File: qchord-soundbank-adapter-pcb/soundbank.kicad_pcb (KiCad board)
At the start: 2 copper layers, 32 x 47.5 mm, 2 parts, among them U1 8MB ROM, U2 8MB Flash

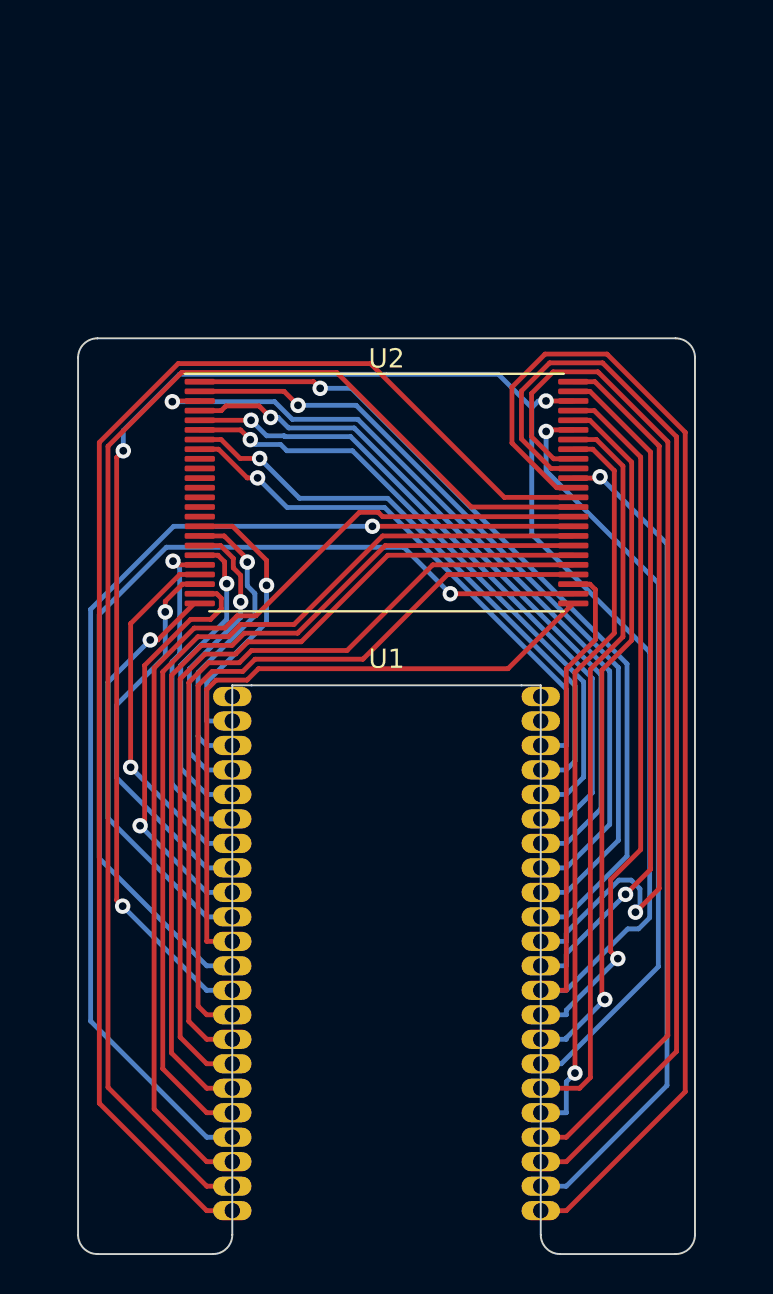
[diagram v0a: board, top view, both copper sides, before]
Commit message: Flip outtie to innie
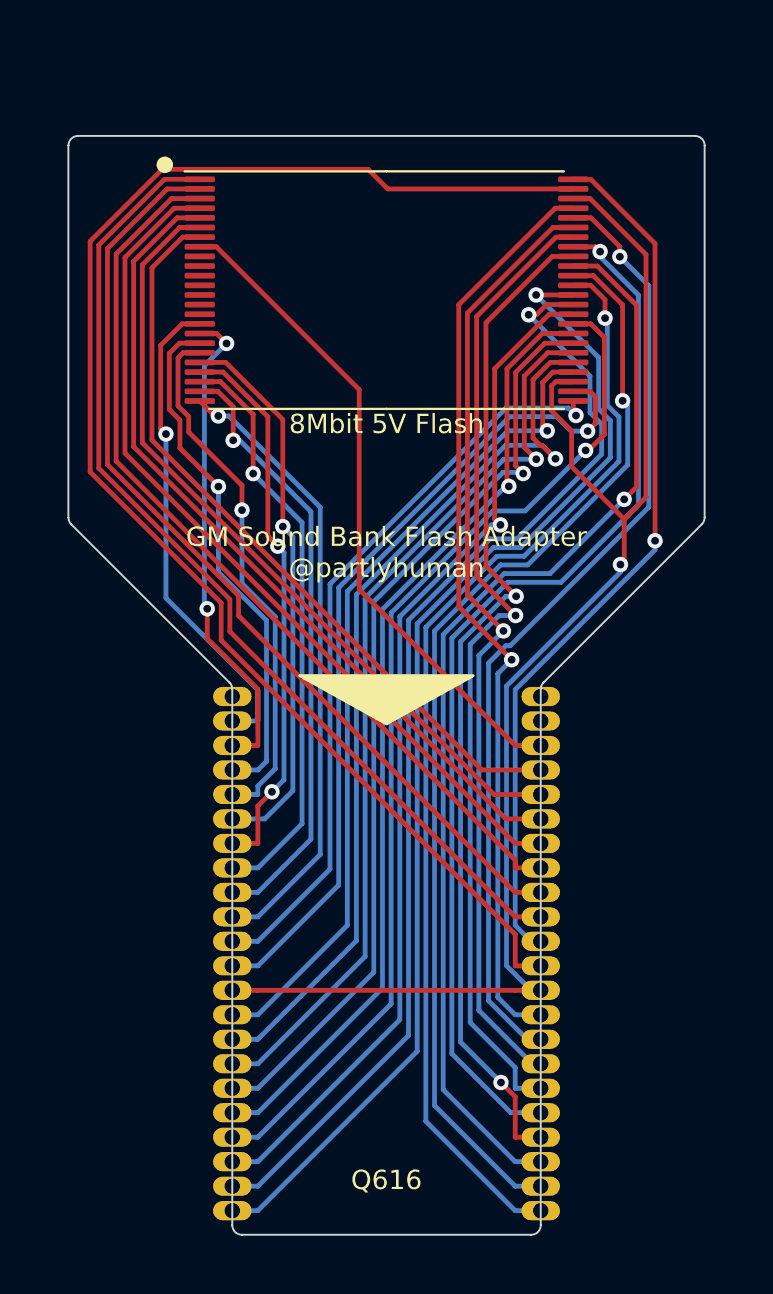
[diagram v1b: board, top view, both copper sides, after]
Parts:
- U2: value 8MB Flash -> 8Mbit 5V Flash
- moved U2 10.5 mm to (94.5, 43.0)
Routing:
- net /GND: track 118.1 -> 72.9 mm, vias 3 -> 1
- net /BYTE: track 35.1 -> 75.1 mm, vias 1 -> 0
- net /Q13: track 38.3 -> 55.4 mm
- net /Q4: track 43.1 -> 57.0 mm
- net /Q7: track 36.7 -> 49.9 mm
- net /Q6: track 38.4 -> 51.4 mm, vias 0 -> 1
- net /Q11: track 72.6 -> 60.7 mm, vias 0 -> 1
- net /Q3: track 70.4 -> 58.8 mm, vias 0 -> 1
- net /A5: track 17.2 -> 28.8 mm
- net /Q15: track 36.7 -> 48.0 mm
- net /A6: track 16.4 -> 27.7 mm
- net /A7: track 16.0 -> 27.0 mm
- net /A1: track 22.1 -> 32.4 mm
- net /A18: track 15.1 -> 25.4 mm
- net /A3: track 20.3 -> 30.3 mm
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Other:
- board size 32 x 47.5 mm -> 33 x 57 mm
- board text added: "GM Sound Bank Flash Adapter @partlyhuman"
- board text added: "Q616"

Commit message: Makes room for neighboring IC
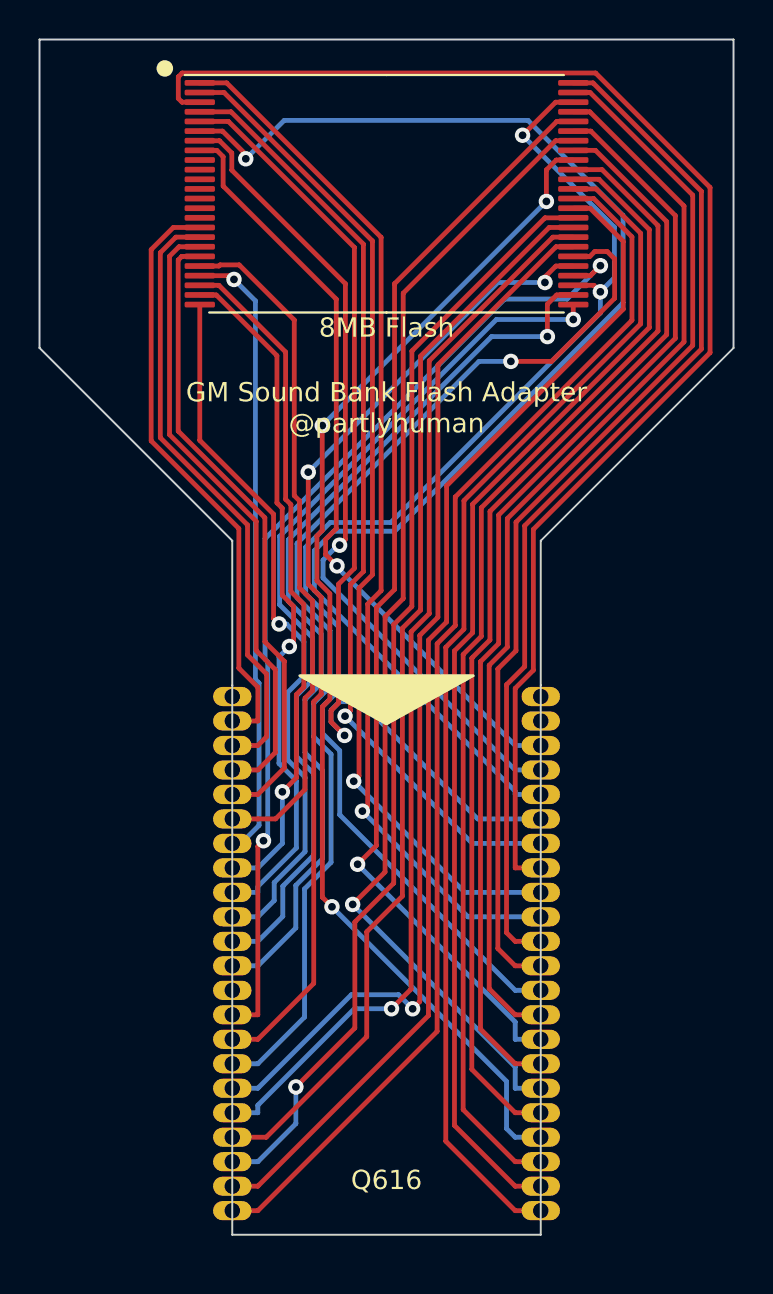
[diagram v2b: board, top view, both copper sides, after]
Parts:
- U2: value 8Mbit 5V Flash -> 8MB Flash
- moved U2 5.00 mm to (94.5, 38.0)
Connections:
- U1 pad 13: /GND -> unconnected-(U1-GND-Pad13)
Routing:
- net /A10: track 41.2 -> 69.7 mm, vias 0 -> 1
- net /A13: track 47.3 -> 73.2 mm
- net /BYTE: track 75.1 -> 54.3 mm
- net /Q8: track 47.3 -> 57.5 mm
- net /Q5: track 52.9 -> 62.6 mm, vias 2 -> 3
- net /A11: track 43.1 -> 52.0 mm, vias 0 -> 1
- net /Q14: track 49.2 -> 57.4 mm, vias 1 -> 0
- net /A16: track 45.7 -> 53.6 mm, vias 1 -> 0
- net /Q6: track 51.4 -> 59.2 mm
- net /Q15: track 48.0 -> 55.8 mm, vias 1 -> 0
- net /OE: track 43.4 -> 51.2 mm, vias 1 -> 2
- net /Q7: track 49.9 -> 57.5 mm
- net /A0: track 38.9 -> 45.6 mm
- net /A5: track 28.8 -> 35.4 mm, vias 1 -> 0
- net /GND: track 72.9 -> 66.2 mm, vias 1 -> 2
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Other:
- board size 33 x 57 mm -> 36 x 62 mm

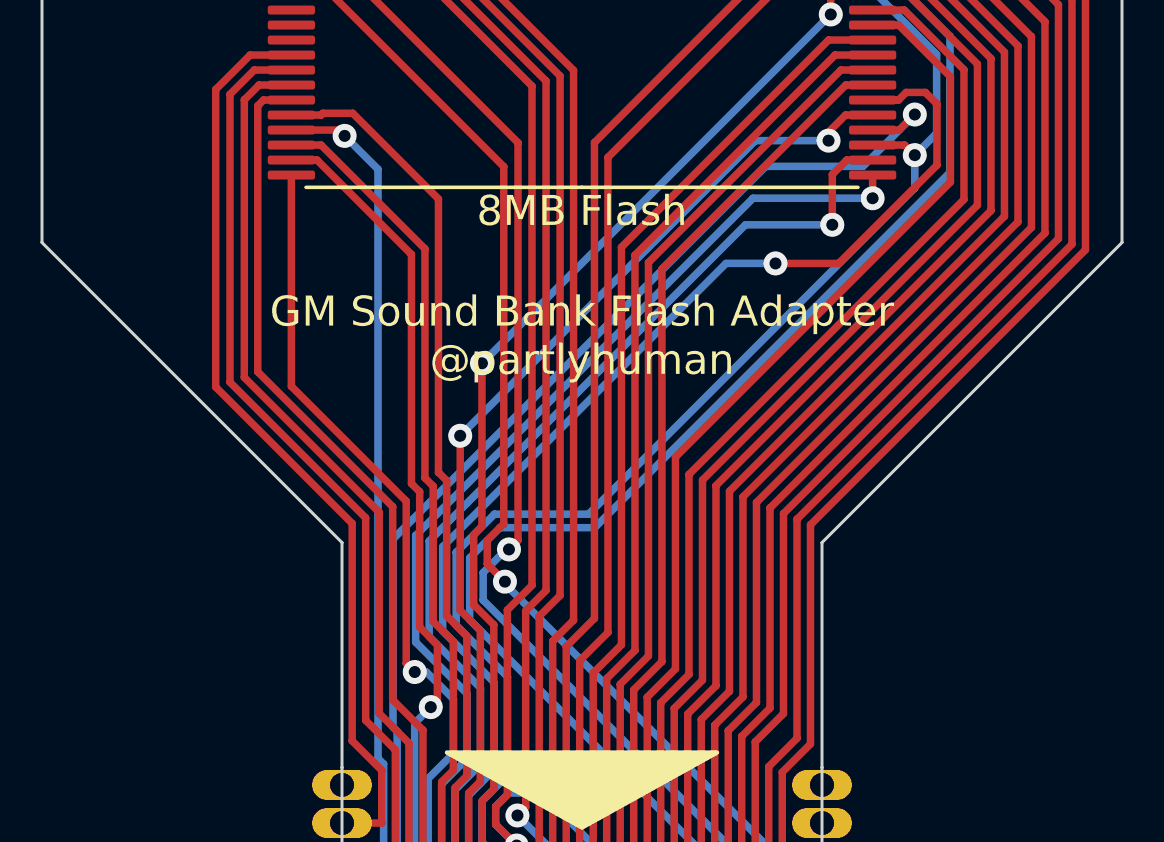
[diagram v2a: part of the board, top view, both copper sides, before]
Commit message: Comic sans to match mainboard
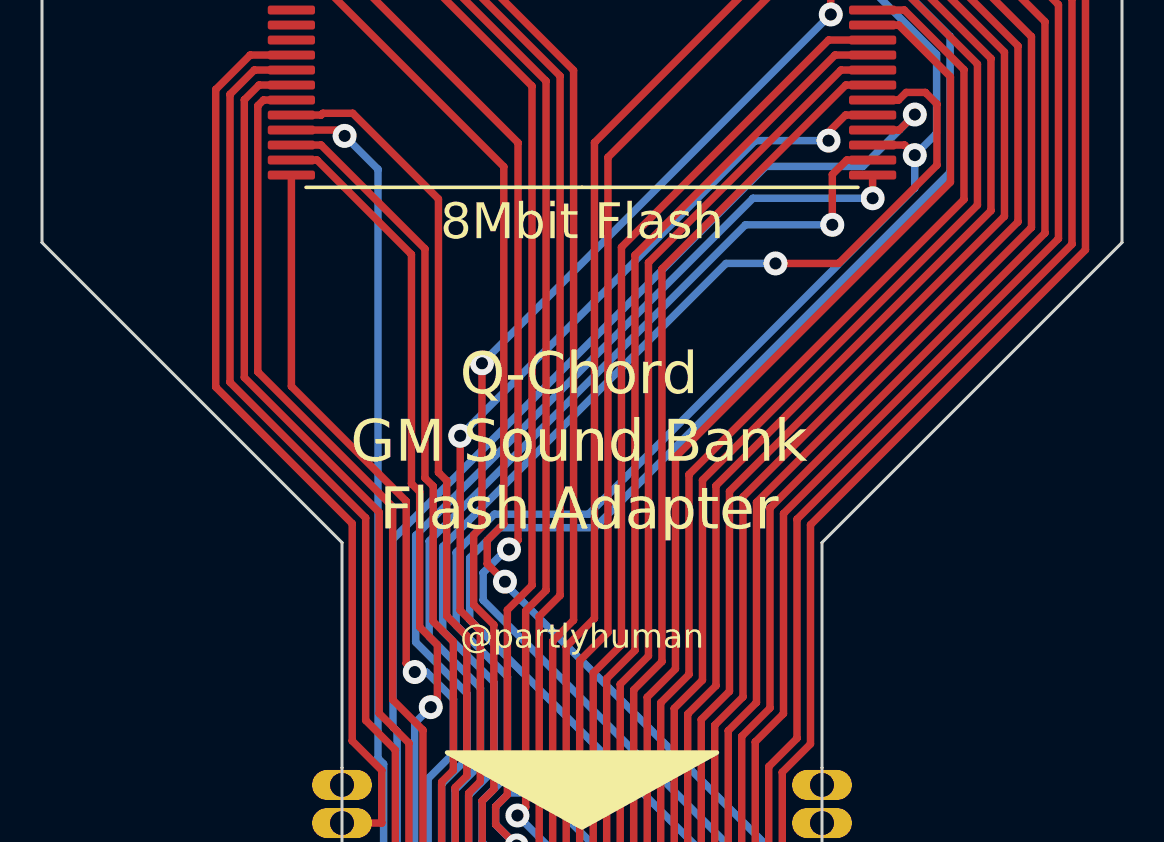
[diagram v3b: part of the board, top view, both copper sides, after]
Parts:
- U2: value 8MB Flash -> 8Mbit Flash
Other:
- board text added: "@partlyhuman"
- board text added: "Q-Chord GM Sound Bank Flash Adapter"
- board text removed: "GM Sound Bank Flash Adapter @partlyhuman"

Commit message: Redesign in-place
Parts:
- moved U2 39.4 mm to (94.5, 77.4), turned to -90 degrees
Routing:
- net /A13: track 73.2 -> 7.75 mm, vias 0 -> 1
- net /A10: track 69.7 -> 6.61 mm
- net /Q5: track 62.6 -> 8.09 mm, vias 3 -> 1
- net /Q11: track 63.7 -> 10.1 mm
- net /Q3: track 61.5 -> 8.95 mm
- net /Q4: track 61.5 -> 9.28 mm
- net /VCC: track 62.2 -> 10.1 mm
- net /Q12: track 60.8 -> 8.85 mm
- net /Q6: track 59.2 -> 7.60 mm
- net /Q13: track 59.0 -> 7.48 mm, vias 0 -> 1
- net /Q10: track 57.9 -> 8.22 mm, vias 1 -> 0
- net /Q7: track 57.5 -> 8.38 mm
- net /Q8: track 57.5 -> 8.63 mm
- net /Q2: track 56.3 -> 8.10 mm
- net /Q1: track 55.2 -> 7.63 mm
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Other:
- board size 36 x 62 mm -> 16 x 29.7 mm

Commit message: Don't leave stuff floating
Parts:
- U1: value 8MB ROM -> 8Mbit ROM
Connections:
- U2 pad 11: unconnected-(U2-~{WE}-Pad11) -> /BYTE
- U2 pad 12: unconnected-(U2-~{RESET}-Pad12) -> /BYTE
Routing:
- net /BYTE: track 11.0 -> 24.2 mm, vias 1 -> 0
- net /A2: track 8.54 -> 14.6 mm, vias 0 -> 1
- net /Q13: track 7.48 -> 13.4 mm
- net /Q5: track 8.09 -> 12.6 mm
- net /Q2: track 8.10 -> 12.2 mm, vias 0 -> 1
- net /Q15: track 9.11 -> 12.0 mm, vias 1 -> 0
- net /A6: track 6.21 -> 9.08 mm, vias 1 -> 0
- net /Q14: track 10.4 -> 7.56 mm, vias 0 -> 1
- net /OE: track 9.27 -> 12.0 mm, vias 1 -> 0
- net /A13: track 7.75 -> 10.2 mm, vias 1 -> 0
- net /GND: track 24.3 -> 22.3 mm
- net /A5: track 8.68 -> 6.93 mm, vias 0 -> 1
- net /Q9: track 8.90 -> 8.03 mm
- net /Q6: track 7.60 -> 8.45 mm
- net /A8: track 7.20 -> 7.96 mm
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
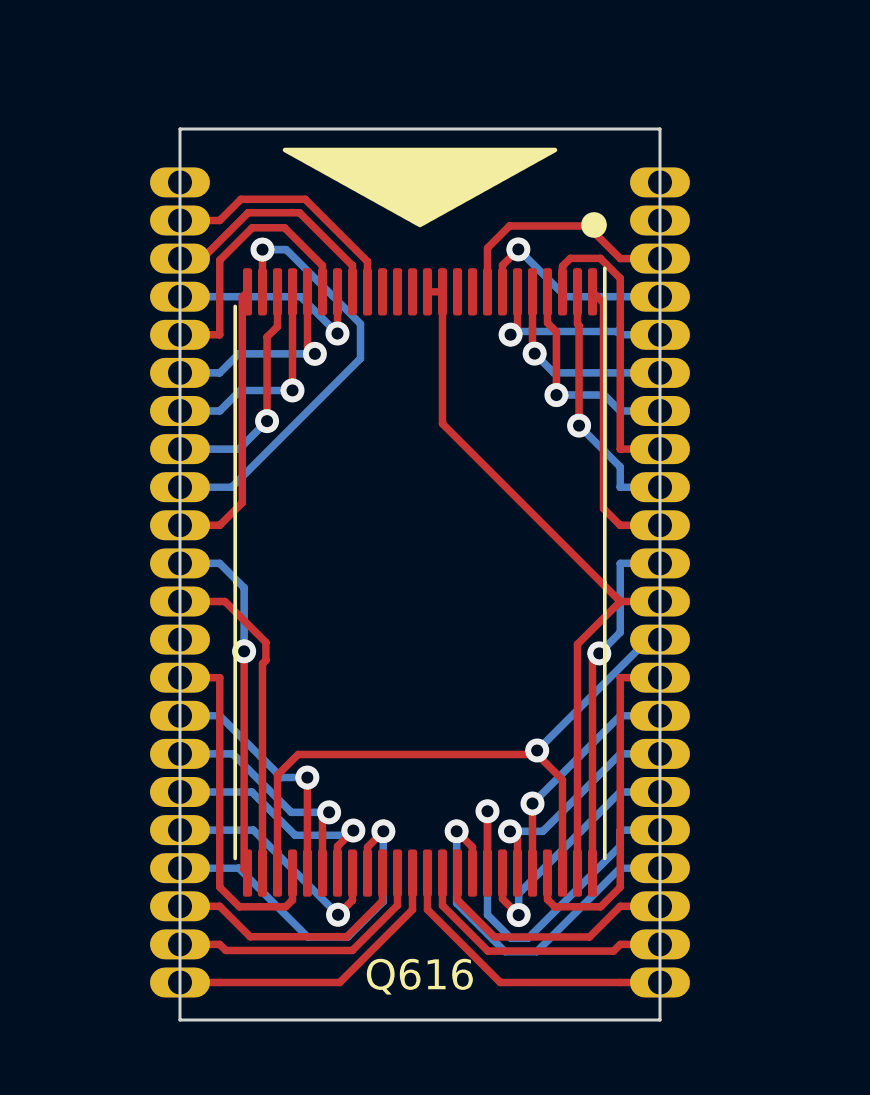
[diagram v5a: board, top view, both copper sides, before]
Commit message: add extra GND
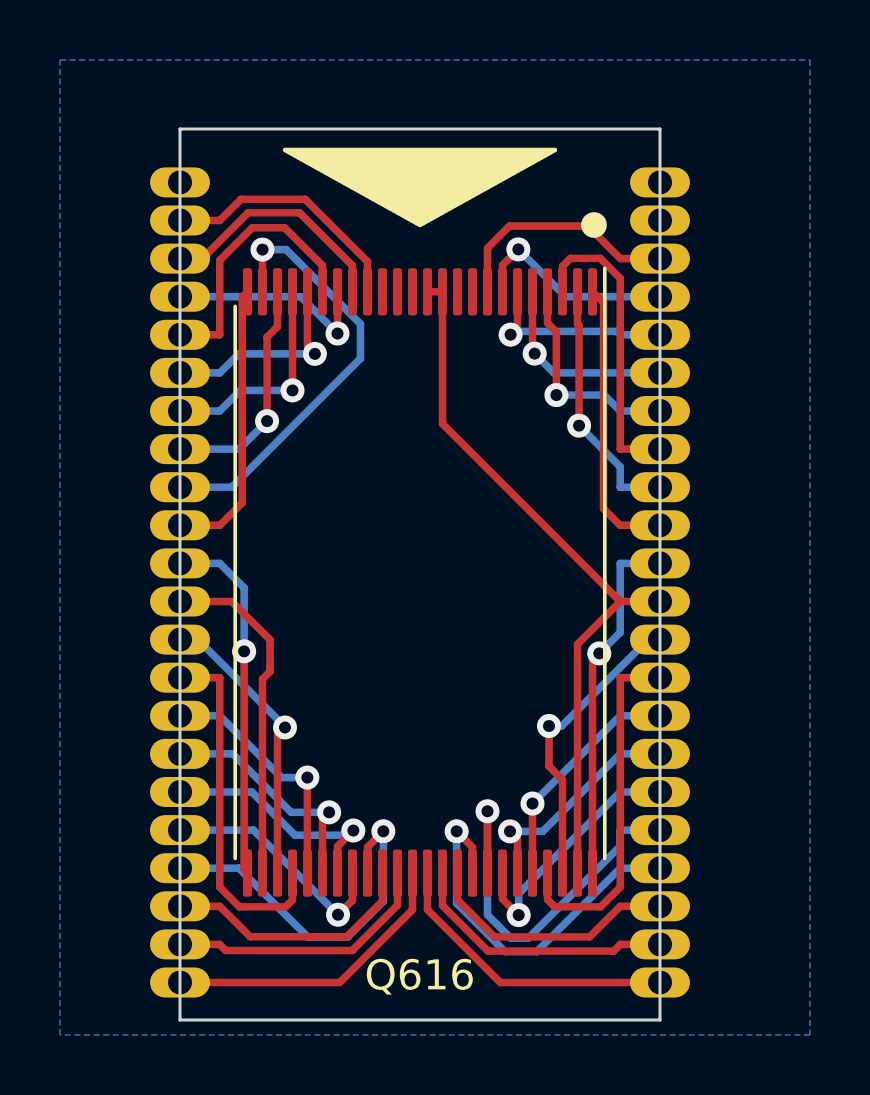
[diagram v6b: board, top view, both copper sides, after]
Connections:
- U1 pad 13: unconnected-(U1-GND-Pad13) -> /GND
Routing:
- net /GND: track 22.3 -> 19.7 mm, vias 1 -> 2
- added copper zone on B.Cu, net /GND
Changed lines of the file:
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@@
   (net 47 "unconnected-(U2-Pad14)")
   (net 48 "unconnected-(U2-~{RY{slash}BY}-Pad15)")
-  (net 49 "unconnected-(U1-GND-Pad13)")
   (footprint "Package_SO:TSOP-I-48_18.4x12mm_P0.5mm" (layer "F.Cu")
     (at 94.5 77.415 -90)
@@
       (net 12 "/CE") (pinfunction "~{CE}") (pintype "input"))
     (pad "13" thru_hole oval (at -8 1.905) (size 2 1) (drill 0.8) (property pad_prop_castellated) (layers "*.Cu" "*.Mask")
-      (net 49 "unconnected-(U1-GND-Pad13)") (pinfunction "GND") (pintype "input+no_connect"))
+      (net 13 "/GND") (pinfunction "GND") (pintype "input"))
     (pad "14" thru_hole oval (at -8 3.175) (size 2 1) (drill 0.8) (property pad_prop_castellated) (layers "*.Cu" "*.Mask")
       (net 14 "/OE") (pinfunction "~{OE}") (pintype "input"))
@@
   (segment (start 86.5 76.78) (end 87.8251 76.78) (width 0.25) (layer "B.Cu") (net 11))
   (segment (start 88.6378 79.712) (end 88.6378 77.5927) (width 0.25) (layer "B.Cu") (net 11))
-  (segment (start 86.5 78.05) (end 87.8251 78.05) (width 0.25) (layer "F.Cu") (net 12))
-  (segment (start 89.25 80.1253) (end 89.3629 80.0124) (width 0.25) (layer "F.Cu") (net 12))
-  (segment (start 89.3629 80.0124) (end 89.3629 79.4116) (width 0.25) (layer "F.Cu") (net 12))
-  (segment (start 89.3629 79.4116) (end 88.0013 78.05) (width 0.25) (layer "F.Cu") (net 12))
-  (segment (start 89.25 87.1025) (end 89.25 80.1253) (width 0.25) (layer "F.Cu") (net 12))
-  (segment (start 88.0013 78.05) (end 87.8251 78.05) (width 0.25) (layer "F.Cu") (net 12))
-  (segment (start 98.4062 83.1494) (end 98.4062 83.0168) (width 0.25) (layer "F.Cu") (net 13))
-  (segment (start 90.4372 83.1494) (end 89.75 83.8366) (width 0.25) (layer "F.Cu") (net 13))
-  (segment (start 99.25 83.9932) (end 98.4062 83.1494) (width 0.25) (layer "F.Cu") (net 13))
-  (segment (start 98.4062 83.1494) (end 90.4372 83.1494) (width 0.25) (layer "F.Cu") (net 13))
-  (segment (start 99.25 87.1025) (end 99.25 83.9932) (width 0.25) (layer "F.Cu") (net 13))
-  (segment (start 89.75 83.8366) (end 89.75 87.1025) (width 0.25) (layer "F.Cu") (net 13))
-  (via (at 98.4062 83.0168) (size 0.8) (drill 0.4) (layers "F.Cu" "B.Cu") (net 13))
-  (segment (start 102.5 79.32) (end 102.103 79.32) (width 0.25) (layer "B.Cu") (net 13))
-  (segment (start 102.103 79.32) (end 98.4062 83.0168) (width 0.25) (layer "B.Cu") (net 13))
+  (segment (start 89.25 87.1025) (end 89.25 80.63765) (width 0.25) (layer "F.Cu") (net 12))
+  (segment (start 88.22565 78.05) (end 86.5 78.05) (width 0.25) (layer "F.Cu") (net 12))
+  (segment (start 89.25 80.63765) (end 89.5 80.38765) (width 0.25) (layer "F.Cu") (net 12))
+  (segment (start 89.5 80.38765) (end 89.5 79.32435) (width 0.25) (layer "F.Cu") (net 12))
+  (segment (start 89.5 79.32435) (end 88.22565 78.05) (width 0.25) (layer "F.Cu") (net 12))
+  (segment (start 90 82.25) (end 89.75 82.5) (width 0.25) (layer "F.Cu") (net 13))
+  (segment (start 99.25 83.9932) (end 99.25 87.1025) (width 0.25) (layer "F.Cu") (net 13))
+  (segment (start 89.75 82.5) (end 89.75 87.1025) (width 0.25) (layer "F.Cu") (net 13))
+  (segment (start 98.8 82.2) (end 98.8 83.5432) (width 0.25) (layer "F.Cu") (net 13))
+  (segment (start 98.8 83.5432) (end 99.25 83.9932) (width 0.25) (layer "F.Cu") (net 13))
+  (via (at 90 82.25) (size 0.8) (drill 0.4) (layers "F.Cu" "B.Cu") (net 13))
+  (via (at 98.8 82.2) (size 0.8) (drill 0.4) (layers "F.Cu" "B.Cu") (net 13))
+  (segment (start 98.8 82.2) (end 99.223 82.2) (width 0.25) (layer "B.Cu") (net 13))
+  (segment (start 87.095718 79.32) (end 86.5 79.32) (width 0.25) (layer "B.Cu") (net 13))
+  (segment (start 99.223 82.2) (end 102.103 79.32) (width 0.25) (layer "B.Cu") (net 13))
+  (segment (start 102.103 79.32) (end 102.5 79.32) (width 0.25) (layer "B.Cu") (net 13))
+  (segment (start 90 82.224282) (end 87.095718 79.32) (width 0.25) (layer "B.Cu") (net 13))
+  (segment (start 90 82.25) (end 90 82.224282) (width 0.25) (layer "B.Cu") (net 13))
   (segment (start 90.25 87.1025) (end 90.25 87.9998) (width 0.25) (layer "F.Cu") (net 14))
   (segment (start 87.8251 87.5733) (end 87.8251 80.59) (width 0.25) (layer "F.Cu") (net 14))
@@
   (segment (start 101.1749 66.62) (end 100.0884 65.5335) (width 0.25) (layer "F.Cu") (net 41))
   (segment (start 102.5 66.62) (end 101.1749 66.62) (width 0.25) (layer "F.Cu") (net 41))
+  (zone (net 13) (net_name "/GND") (layer "B.Cu") (hatch edge 0.5)
+    (connect_pads (clearance 0.5))
+    (min_thickness 0.25) (filled_areas_thickness no)
+    (fill yes (thermal_gap 0.5) (thermal_bridge_width 0.5))
+    (polygon
+      (pts
+        (xy 82.5 60)
+        (xy 107.5 60)
+        (xy 107.5 92.5)
+        (xy 82.5 92.5)
+      )
+    )
+  )
 )
